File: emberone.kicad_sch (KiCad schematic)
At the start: 18 parts, among them J1 Screw Terminal, J2 Screw Terminal, U11 256 Foundation Logo, U12 70x90mm Heatsink

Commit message: added RI pullup resistors for #16. updated BOM. bumped version number to 3
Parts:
- EXTRA1: renamed from U12; now left out of the parts list
- LOGO1: renamed from U11; now left out of the parts list
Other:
- title: emberOne -> emberOne/00
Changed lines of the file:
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@@
 	(paper "A3")
 	(title_block
-		(title "emberOne")
-		(date "2024-11-25")
-		(rev "2")
+		(title "emberOne/00")
+		(date "2025-02-25")
+		(rev "3")
 	)
 	(junction
@@
 		(unit 1)
 		(exclude_from_sim no)
-		(in_bom yes)
+		(in_bom no)
 		(on_board yes)
 		(dnp no)
 		(fields_autoplaced yes)
-		(property "Reference" "U11"
+		(property "Reference" "LOGO1"
 			(at 350.52 250.19 0)
 			(effects
@@
 			(project ""
 				(path "/b036224c-4cdf-48cc-81df-19bc5283ebd2"
-					(reference "U11")
+					(reference "LOGO1")
 					(unit 1)
 				)
@@
 		(unit 1)
 		(exclude_from_sim no)
-		(in_bom yes)
+		(in_bom no)
 		(on_board yes)
 		(dnp no)
 		(fields_autoplaced yes)
-		(property "Reference" "U12"
+		(property "Reference" "EXTRA1"
 			(at 350.52 246.38 0)
 			(effects
@@
 			(project ""
 				(path "/b036224c-4cdf-48cc-81df-19bc5283ebd2"
-					(reference "U12")
+					(reference "EXTRA1")
 					(unit 1)
 				)

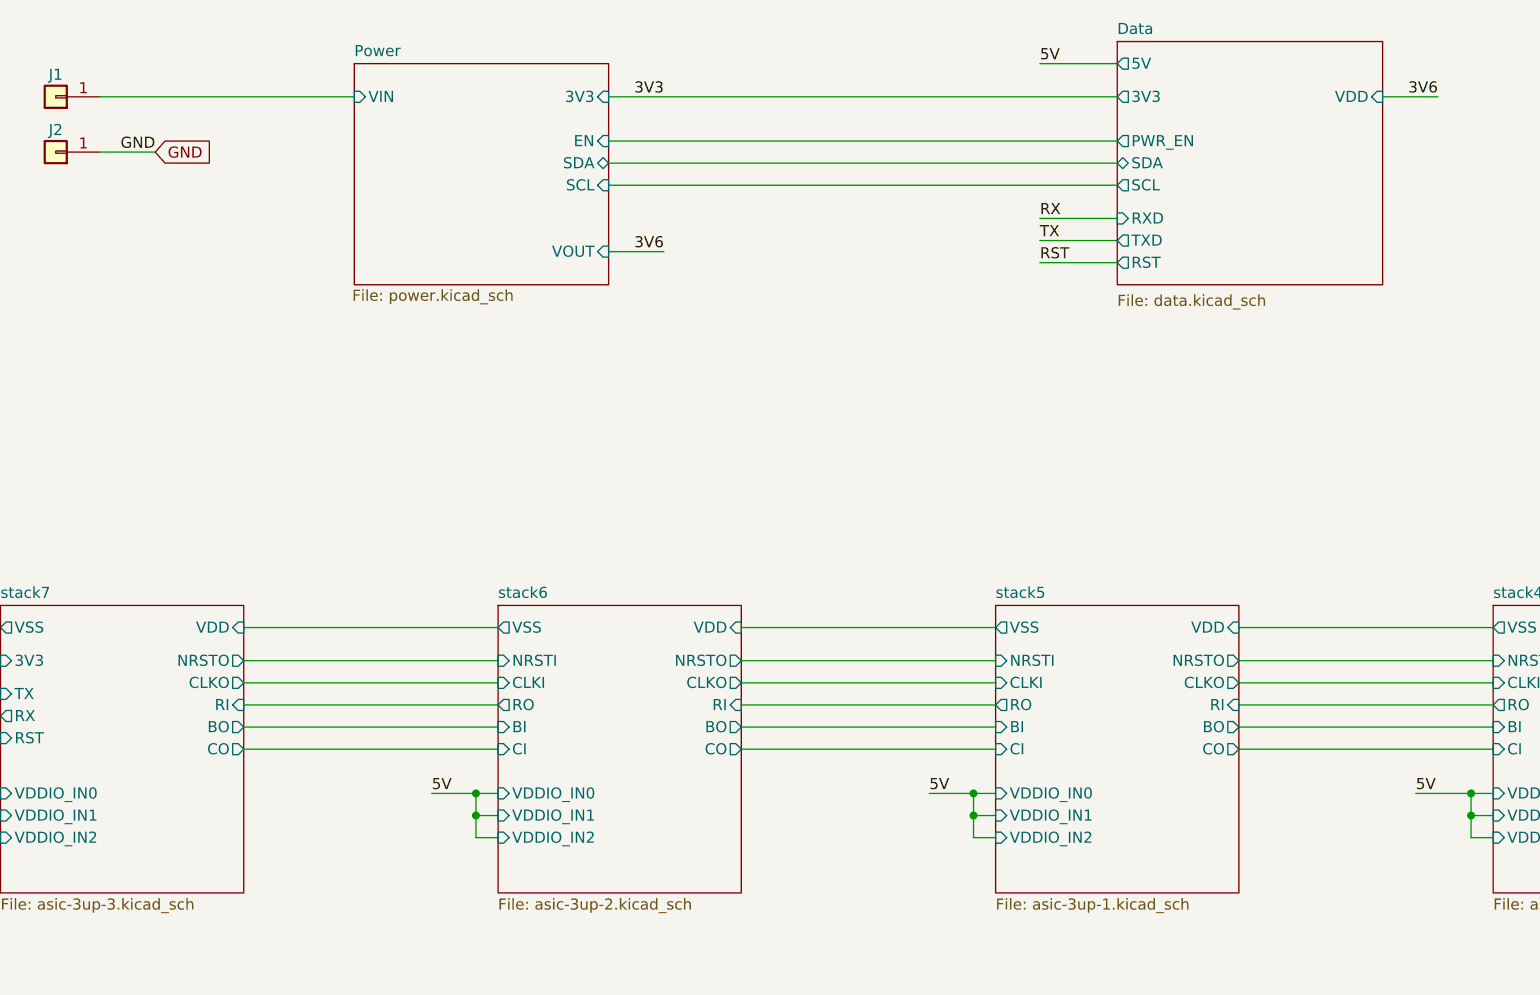
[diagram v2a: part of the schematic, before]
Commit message: added thermal diode reader for #34. reconfigured power tracks to be on both top and bottom layers
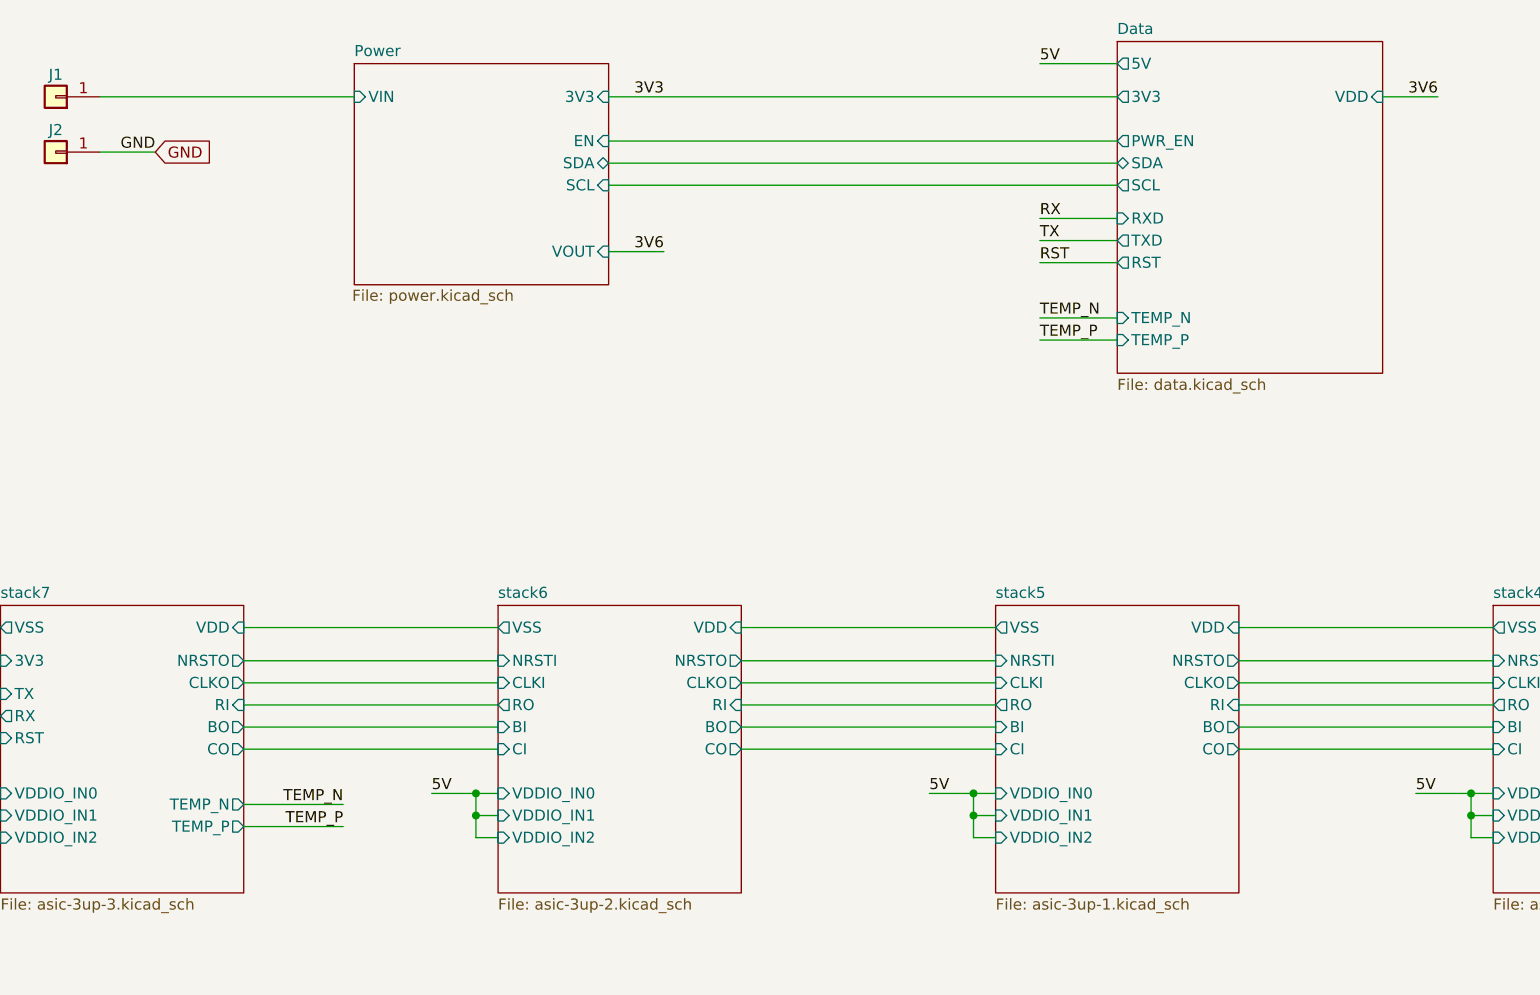
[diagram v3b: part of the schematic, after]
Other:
- sheet Data ports: added TEMP_N, TEMP_P; removed none
- sheet stack7 ports: added TEMP_N, TEMP_P; removed none
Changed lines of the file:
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@@
+	(wire
+		(pts
+			(xy 229.87 107.95) (xy 238.76 107.95)
+		)
+		(stroke
+			(width 0)
+			(type default)
+		)
+	)
 	(wire
 		(pts
@@
 	(wire
 		(pts
+			(xy 229.87 110.49) (xy 238.76 110.49)
+		)
+		(stroke
+			(width 0)
+			(type default)
+		)
+	)
+	(wire
+		(pts
 			(xy 279.4 165.1) (xy 279.4 162.56)
 		)
@@
 	(wire
 		(pts
+			(xy 138.43 163.83) (xy 149.86 163.83)
+		)
+		(stroke
+			(width 0)
+			(type default)
+		)
+	)
+	(wire
+		(pts
 			(xy 224.79 165.1) (xy 222.25 165.1)
 		)
@@
 		(pts
 			(xy 107.95 162.56) (xy 110.49 162.56)
+		)
+		(stroke
+			(width 0)
+			(type default)
+		)
+	)
+	(wire
+		(pts
+			(xy 138.43 166.37) (xy 149.86 166.37)
 		)
 		(stroke
@@
 		)
 	)
+	(label "TEMP_N"
+		(at 149.86 163.83 180)
+		(effects
+			(font
+				(size 1.27 1.27)
+			)
+			(justify right bottom)
+		)
+	)
 	(label "GND"
 		(at 128.27 88.9 180)
@@
 		)
 	)
+	(label "TEMP_P"
+		(at 229.87 110.49 0)
+		(effects
+			(font
+				(size 1.27 1.27)
+			)
+			(justify left bottom)
+		)
+	)
 	(label "RX"
 		(at 229.87 96.52 0)
@@
 			)
 			(justify left bottom)
+		)
+	)
+	(label "TEMP_N"
+		(at 229.87 107.95 0)
+		(effects
+			(font
+				(size 1.27 1.27)
+			)
+			(justify left bottom)
+		)
+	)
+	(label "TEMP_P"
+		(at 149.86 166.37 180)
+		(effects
+			(font
+				(size 1.27 1.27)
+			)
+			(justify right bottom)
 		)
 	)
@@
 			)
 		)
+		(pin "TEMP_N" output
+			(at 138.43 163.83 0)
+			(effects
+				(font
+					(size 1.27 1.27)
+				)
+				(justify right)
+			)
+		)
+		(pin "TEMP_P" output
+			(at 138.43 166.37 0)
+			(effects
+				(font
+					(size 1.27 1.27)
+				)
+				(justify right)
+			)
+		)
 		(instances
 			(project "emberone"
@@
 	(sheet
 		(at 238.76 76.2)
-		(size 30.48 27.94)
+		(size 30.48 38.1)
 		(exclude_from_sim no)
 		(in_bom yes)
@@
 		)
 		(property "Sheetfile" "data.kicad_sch"
-			(at 238.76 105.2326 0)
+			(at 238.76 114.8846 0)
 			(effects
 				(font
@@
 			)
 		)
+		(pin "TEMP_N" input
+			(at 238.76 107.95 180)
+			(effects
+				(font
+					(size 1.27 1.27)
+				)
+				(justify left)
+			)
+		)
+		(pin "TEMP_P" input
+			(at 238.76 110.49 180)
+			(effects
+				(font
+					(size 1.27 1.27)
+				)
+				(justify left)
+			)
+		)

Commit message: switched to right angle power screw terminals. moved TMP1075 temp sensor to clear heatsink for #44
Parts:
- J1, J2: footprint emberone:7770-screw-terminal -> emberone:7790-RA-screw-terminal; DK 36-7770-ND -> 36-7790-ND; PARTNO 36-7770 -> 7790
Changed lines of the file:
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@@
 			)
 		)
-		(property "Footprint" "emberone:7770-screw-terminal"
+		(property "Footprint" "emberone:7790-RA-screw-terminal"
 			(at 116.84 82.55 0)
 			(effects
@@
 			)
 		)
-		(property "Datasheet" "https://mm.digikey.com/Volume0/opasdata/d220001/medias/docus/581/Metric_PCB_Screw_Terminals.pdf"
+		(property "Datasheet" "https://www.keyelco.com/userAssets/file/M65p69.pdf"
 			(at 116.84 82.55 0)
 			(effects
@@
 			)
 		)
-		(property "DK" "36-7770-ND"
+		(property "DK" "36-7790-ND"
 			(at 116.84 82.55 0)
 			(effects
@@
 			)
 		)
-		(property "PARTNO" "36-7770"
+		(property "PARTNO" "7790"
 			(at 116.84 82.55 0)
 			(effects
@@
 			)
 		)
-		(property "Footprint" "emberone:7770-screw-terminal"
+		(property "Footprint" "emberone:7790-RA-screw-terminal"
 			(at 116.84 88.9 0)
 			(effects
@@
 			)
 		)
-		(property "DK" "36-7770-ND"
+		(property "DK" "36-7790-ND"
 			(at 116.84 88.9 0)
 			(effects
@@
 			)
 		)
-		(property "PARTNO" "36-7770"
+		(property "PARTNO" "7790"
 			(at 116.84 88.9 0)
 			(effects
